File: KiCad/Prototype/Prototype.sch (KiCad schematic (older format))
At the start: 25 parts, among them IC1 ATMEGA328-P, P1 CONN_01X02, P2 CONN_01X02, P3 CONN_01X03, P4 CONN_01X02, P6 CONN_01X02, SW2 SW_PUSH, SW6 SW_PUSH, SW7 SW_PUSH, U1 LM317AT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

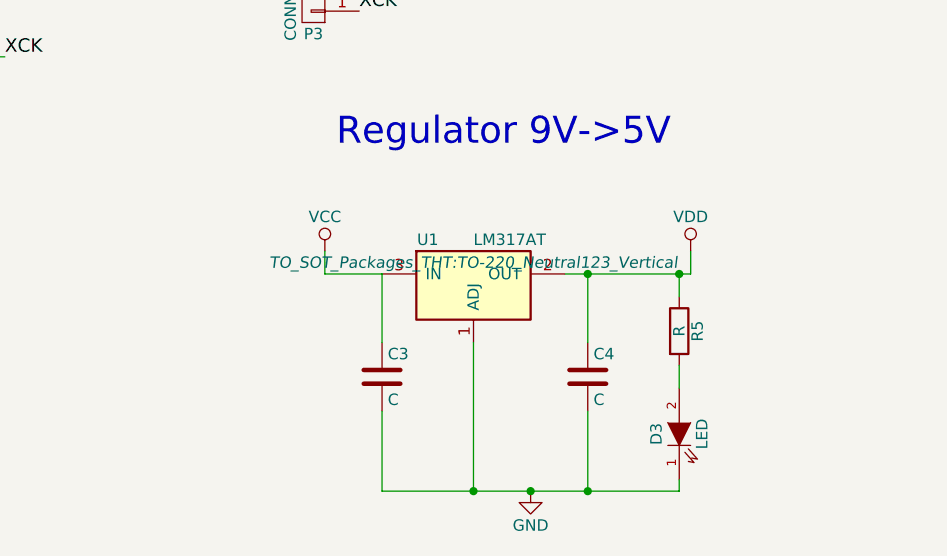
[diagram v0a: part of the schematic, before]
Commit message: Switched LM317 to 7805 and fixed pcb
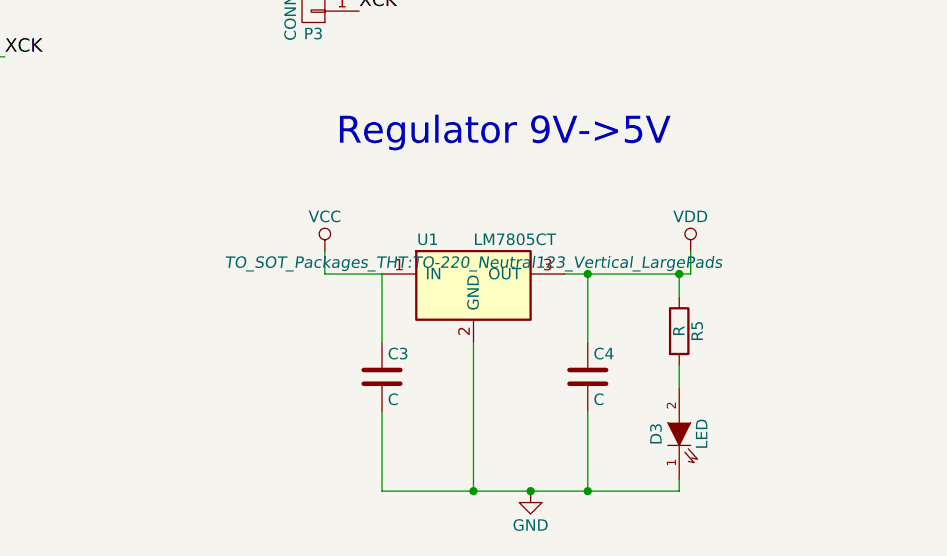
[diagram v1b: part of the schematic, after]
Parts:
- removed U1: LM317AT, TO_SOT_Packages_THT:TO-220_Neutral123_Vertical, symbol LM317AT
- added U1: LM7805CT, TO_SOT_Packages_THT:TO-220_Neutral123_Vertical_LargePads, symbol LM7805CT
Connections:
- net GND: now also U1.2 (GND)
- net VCC: now also U1.1 (IN)
- net VDD: now also U1.3 (OUT)
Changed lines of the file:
@@
 	-1   0    0    1
-$EndComp
-$Comp
-L LM317AT U1
-U 1 1 582BDC14
-P 6100 9900
-F 0 "U1" H 5900 10100 50  0000 C CNN
-F 1 "LM317AT" H 6100 10100 50  0000 L CNN
-F 2 "TO_SOT_Packages_THT:TO-220_Neutral123_Vertical" H 6100 10000 50  0000 C CIN
-F 3 "" H 6100 9900 50  0000 C CNN
-	1    6100 9900
-	1    0    0    -1
 $EndComp
 NoConn ~ 3750 8050
@@
 Text Label 3750 8250 0    59   ~ 0
 PED_2
+$Comp
+L LM7805CT U1
+U 1 1 582EDB19
+P 6100 9900
+F 0 "U1" H 5900 10100 50  0000 C CNN
+F 1 "LM7805CT" H 6100 10100 50  0000 L CNN
+F 2 "TO_SOT_Packages_THT:TO-220_Neutral123_Vertical_LargePads" H 6100 10000 50  0000 C CIN
+F 3 "" H 6100 9900 50  0000 C CNN
+	1    6100 9900
+	1    0    0    -1
+$EndComp
 $EndSCHEMATC

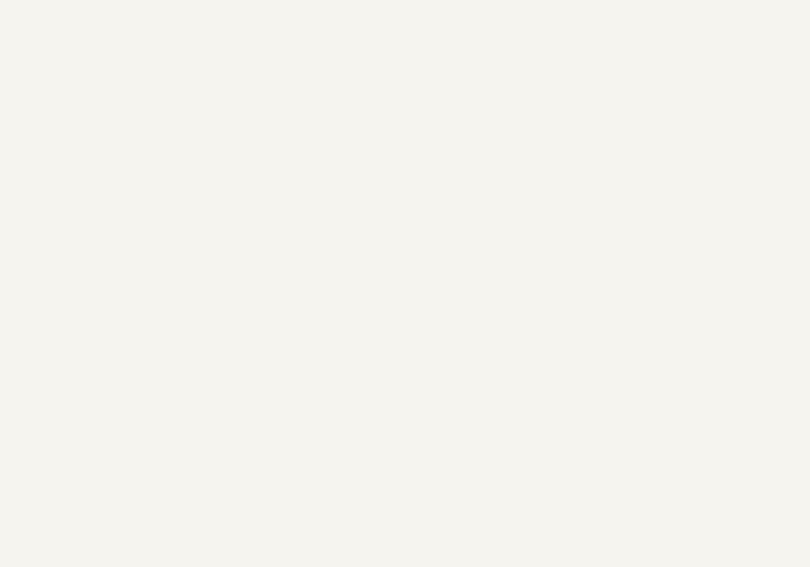
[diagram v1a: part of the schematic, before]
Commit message: Perfected prototype and added a guitar amp switch prototype
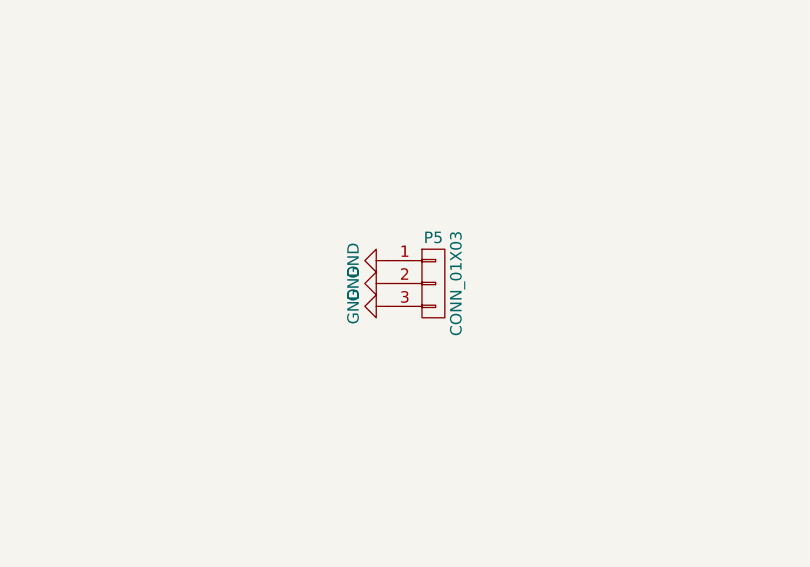
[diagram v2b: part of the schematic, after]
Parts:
- added P5: CONN_01X03, Connectors_Molex:Molex_KK-6410-03_03x2.54mm_Straight, symbol CONN_01X03
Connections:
- net GND: now also P5.1 (P1), P5.2 (P2), P5.3 (P3)
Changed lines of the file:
@@
 	1    0    0    -1
 $EndComp
+$Comp
+L CONN_01X03 P5
+U 1 1 5835BDCB
+P 12200 3850
+F 0 "P5" H 12200 4050 50  0000 C CNN
+F 1 "CONN_01X03" V 12300 3850 50  0000 C CNN
+F 2 "Connectors_Molex:Molex_KK-6410-03_03x2.54mm_Straight" H 12200 3850 50  0001 C CNN
+F 3 "" H 12200 3850 50  0000 C CNN
+	1    12200 3850
+	1    0    0    -1
+$EndComp
+$Comp
+L GND #PWR020
+U 1 1 5835BE3A
+P 12000 3950
+F 0 "#PWR020" H 12000 3700 50  0001 C CNN
+F 1 "GND" H 12000 3800 50  0000 C CNN
+F 2 "" H 12000 3950 50  0000 C CNN
+F 3 "" H 12000 3950 50  0000 C CNN
+	1    12000 3950
+	0    1    1    0
+$EndComp
+$Comp
+L GND #PWR021
+U 1 1 5835C73A
+P 12000 3850
+F 0 "#PWR021" H 12000 3600 50  0001 C CNN
+F 1 "GND" H 12000 3700 50  0000 C CNN
+F 2 "" H 12000 3850 50  0000 C CNN
+F 3 "" H 12000 3850 50  0000 C CNN
+	1    12000 3850
+	0    1    1    0
+$EndComp
+$Comp
+L GND #PWR022
+U 1 1 5835C793
+P 12000 3750
+F 0 "#PWR022" H 12000 3500 50  0001 C CNN
+F 1 "GND" H 12000 3600 50  0000 C CNN
+F 2 "" H 12000 3750 50  0000 C CNN
+F 3 "" H 12000 3750 50  0000 C CNN
+	1    12000 3750
+	0    1    1    0
+$EndComp
 $EndSCHEMATC
